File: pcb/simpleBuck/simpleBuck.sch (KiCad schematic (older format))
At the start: 55 parts

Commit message: Made lm2596 breakout board.
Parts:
- removed C? (x13): C, symbol Device:C
- removed D?: D_Zener, symbol Device:D_Zener
- removed D? (x3): D, symbol Device:D
- removed D?: INOLUX_IN-S63BTG, LEDs:LED_0603, symbol DBLS_Diode:INOLUX_IN-S63BTG
- removed J? (x3): Conn_01x02, symbol Connector_Generic:Conn_01x02
- removed L?: L, symbol Device:L
- removed Q?: Q_PMOS_GDS, symbol Device:Q_PMOS_GDS
- removed R?: SMD-RES-10K-0603, Resistors_SMD:R_0603, symbol DBLS_Resistor:SMD-RES-10K-0603
- removed R?: SMD-RES-0-0603, Resistors_SMD:R_0603, symbol DBLS_Resistor:SMD-RES-0-0603
- removed R? (x21): R, symbol Device:R
- removed RV? (x2): R_POT, symbol Device:R_POT
- removed SW?: SW_Push_SPDT, symbol Switch:SW_Push_SPDT
- removed U?: OP07, symbol Amplifier_Operational:OP07
- removed U?: LM2596S-ADJ, Package_TO_SOT_SMD:TO-263-5_TabPin3, symbol Regulator_Switching:LM2596S-ADJ
- removed U? (x3): LM2904, symbol Amplifier_Operational:LM2904
- removed U?: LP5912, DBLS_SON:WSON-6-1EP_2x2mm_P0.65mm_EP1x1.6mm_ThermalVias, symbol DBLS_LDO:LP5912
- added C? (x8): C, symbol Device:C
- added C?: PANASONIC_EEV-FK1J471M, Capacitors_SMD:CP_Elec_10x10.5, symbol DBLS_Capacitor:PANASONIC_EEV-FK1J471M
- added D? (x2): D, symbol Device:D
- added D?: ROHM_RSX501LAM20TR, Diodes_SMD:D_SMB_Handsoldering, symbol DBLS_Diode:ROHM_RSX501LAM20TR
- added D?: D_Zener, symbol Device:D_Zener
- added J? (x2): Conn_01x02, symbol Connector_Generic:Conn_01x02
- added L?: BOURNS_SRR1260A-330M, Inductors_SMD:L_12x12mm_h8mm, symbol DBLS_Inductor:BOURNS_SRR1260A-330M
- added Q?: Q_PMOS_GDS, symbol Device:Q_PMOS_GDS
- added R?: SMD-RES-0-0603, Resistors_SMD:R_0603, symbol DBLS_Resistor:SMD-RES-0-0603
- added R? (x20): R, symbol Device:R
- added R? (x2): VISHAYDALE_CRCW04020000Z0EDHP, Resistors_SMD:R_0402, symbol DBLS_Resistor:VISHAYDALE_CRCW04020000Z0EDHP
- added R?: SMD-RES-10K-0603, Resistors_SMD:R_0603, symbol DBLS_Resistor:SMD-RES-10K-0603
- added RV? (x2): R_POT, symbol Device:R_POT
- added SW?: SW_Push_SPDT, symbol Switch:SW_Push_SPDT
- added U?: LM2596S-ADJ, Package_TO_SOT_SMD:TO-263-5_TabPin3, symbol Regulator_Switching:LM2596S-ADJ
- added U? (x3): LM2904, symbol Amplifier_Operational:LM2904
- added U?: INA194, Package_TO_SOT_SMD:SOT-23-5, symbol Amplifier_Current:INA194
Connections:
- wire segments 126 -> 120
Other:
- note added: "-footprint is wrong\n-Backup cap??"
- note added: "D/L Footprints are close, \nbut not done\n"

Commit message: v1 - placed order with OSH park
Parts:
- removed C? (x8): C, symbol Device:C
- removed C?: PANASONIC_EEV-FK1J471M, Capacitors_SMD:CP_Elec_10x10.5, symbol DBLS_Capacitor:PANASONIC_EEV-FK1J471M
- removed D? (x2): D, symbol Device:D
- removed D?: ROHM_RSX501LAM20TR, Diodes_SMD:D_SMB_Handsoldering, symbol DBLS_Diode:ROHM_RSX501LAM20TR
- removed J?: Conn_01x02, symbol Connector_Generic:Conn_01x02
- removed L?: BOURNS_SRR1260A-330M, Inductors_SMD:L_12x12mm_h8mm, symbol DBLS_Inductor:BOURNS_SRR1260A-330M
- removed R?: SMD-RES-0-0603, Resistors_SMD:R_0603, symbol DBLS_Resistor:SMD-RES-0-0603
- removed R? (x20): R, symbol Device:R
- removed R? (x2): VISHAYDALE_CRCW04020000Z0EDHP, Resistors_SMD:R_0402, symbol DBLS_Resistor:VISHAYDALE_CRCW04020000Z0EDHP
- removed RV? (x2): R_POT, symbol Device:R_POT
- removed SW?: SW_Push_SPDT, symbol Switch:SW_Push_SPDT
- removed U?: LM2596S-ADJ, Package_TO_SOT_SMD:TO-263-5_TabPin3, symbol Regulator_Switching:LM2596S-ADJ
- removed U? (x3): LM2904, symbol Amplifier_Operational:LM2904
- removed U?: INA194, Package_TO_SOT_SMD:SOT-23-5, symbol Amplifier_Current:INA194
- added R?: STACKPOLE_CSRT2512FT50L0-UP, Resistors_SMD:R_2512, symbol DBLS_Resistor:STACKPOLE_CSRT2512FT50L0-UP
- added TP? (x2): DBLS_TESTPOINT_NORMAL, DBLS_Misc:DBLS_Testpoint_Normal, symbol DBLS_Misc:DBLS_TESTPOINT_NORMAL
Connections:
- net labels added: VBUS
- net labels removed: +5V, I_SENSE, VIN_PROT, VOUT, V_FB
- wire segments 120 -> 16
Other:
- note removed: "-footprint is wrong\n-Backup cap??"
- note removed: "D/L Footprints are close, \nbut not done\n"
- note removed: "EXTERNAL SWITCH"
- note removed: "SHOULD THIS BE 5V?"
- moved on the sheet: J?

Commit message: Added lm2596 and DACS + prelim layout.
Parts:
- removed D?: D_Zener, symbol Device:D_Zener
- removed J?: Conn_01x02, symbol Connector_Generic:Conn_01x02
- removed Q?: Q_PMOS_GDS, symbol Device:Q_PMOS_GDS
- removed R?: SMD-RES-10K-0603, Resistors_SMD:R_0603, symbol DBLS_Resistor:SMD-RES-10K-0603
- removed R?: STACKPOLE_CSRT2512FT50L0-UP, Resistors_SMD:R_2512, symbol DBLS_Resistor:STACKPOLE_CSRT2512FT50L0-UP
- removed TP? (x2): DBLS_TESTPOINT_NORMAL, DBLS_Misc:DBLS_Testpoint_Normal, symbol DBLS_Misc:DBLS_TESTPOINT_NORMAL
- added C1, C2: MURATA_GRT31CR61H106KE01L, Capacitors_SMD:C_1206, symbol DBLS_Capacitor:MURATA_GRT31CR61H106KE01L
- added C10, C11, C17, C18, C19, C20, C8, C9: MURATA_GCJ188R91H104KA01D, Capacitors_SMD:C_0603, symbol DBLS_Capacitor:MURATA_GCJ188R91H104KA01D
- added C12, C13, C3, C4, C5, C6: KEMET_C0603C103K5RAL7867, Capacitors_SMD:C_0603, symbol DBLS_Capacitor:KEMET_C0603C103K5RAL7867
- added C14: RUBYCON_100ZLH100MEFC10X20, Capacitors_THT:CP_Radial_D10.0mm_P5.00mm, symbol DBLS_Capacitor:RUBYCON_100ZLH100MEFC10X20
- added C15: MURATA_GCM155R71E103KA37D, Capacitors_SMD:C_0402, symbol DBLS_Capacitor:MURATA_GCM155R71E103KA37D
- added C16: PANASONIC_EEU-FC1H221B, Capacitors_THT:CP_Radial_D10.0mm_P5.00mm, symbol DBLS_Capacitor:PANASONIC_EEU-FC1H221B
- added C7: MURATA_KRM55WR7YA476MH01L, Capacitors_SMD:C_2220, symbol DBLS_Capacitor:MURATA_KRM55WR7YA476MH01L
- added D1, D2, D3: MICRO_COMMERCIAL_1N4148X-TP, LEDs:LED_0603, symbol DBLS_Diode:MICRO_COMMERCIAL_1N4148X-TP
- added D4: VISHAY_SSA34HE3_A_I, Diodes_SMD:D_SMA, symbol DBLS_Diode:VISHAY_SSA34HE3_A_I
- added J1, J3: Conn_01x04, Pin_Headers:Pin_Header_Straight_1x04_Pitch2.54mm, symbol Connector_Generic:Conn_01x04
- added J2: Conn_01x06, Pin_Headers:Pin_Header_Straight_1x06_Pitch2.54mm, symbol Connector_Generic:Conn_01x06
- added J4, J5, J6: Conn_01x02, Pin_Headers:Pin_Header_Straight_1x02_Pitch2.54mm, symbol Connector_Generic:Conn_01x02
- added JP1: PAD_JUMPER_2PIN_NC, DBLS_Misc:PAD_JUMPER_2PIN_NC, symbol DBLS_Misc:PAD_JUMPER_2PIN_NC
- added JP2, JP3, JP4, JP5, JP6, JP7, JP8: PAD_JUMPER_2PIN_0603, DBLS_Misc:PAD_JUMPER_2PIN_0603, symbol DBLS_Misc:PAD_JUMPER_2PIN_0603
- added L1: BOURNS_SRR1260A-330M, Inductors_SMD:L_12x12mm_h8mm, symbol DBLS_Inductor:BOURNS_SRR1260A-330M
- added Q1: TRANSISTOR_PNPMMBT4403, TO_SOT_Packages_SMD:SOT-23, symbol SparkFun-DiscreteSemi:TRANSISTOR_PNPMMBT4403
- added R1, R10, R2, R3, R6: VISHAYDALE_CRCW04021M00FKEDC, Resistors_SMD:R_0402, symbol DBLS_Resistor:VISHAYDALE_CRCW04021M00FKEDC
- added R11: SMD-RES-1.0K-0603, Resistors_SMD:R_0603, symbol DBLS_Resistor:SMD-RES-1.0K-0603
- added R12: VISHAYDALE_CRCW0402150KFKEDC, Resistors_SMD:R_0402, symbol DBLS_Resistor:VISHAYDALE_CRCW0402150KFKEDC
- added R13: STACKPOLE_CSRT2512FT50L0-UP, Resistors_SMD:R_2512, symbol DBLS_Resistor:STACKPOLE_CSRT2512FT50L0-UP
- added R14: VISHAYDALE_CRCW040268K0FKEDC, Resistors_SMD:R_0402, symbol DBLS_Resistor:VISHAYDALE_CRCW040268K0FKEDC
- added R4, R5, R7, R8, R9: VISHAY_CRCW060310K0FKEBC, Resistors_SMD:R_0603, symbol DBLS_Resistor:VISHAY_CRCW060310K0FKEBC
- added RV1, RV2: BOURNS_PV37W203C01B00, Potentiometers:Potentiometer_Trimmer_Bourns_3299Y, symbol DBLS_Resistor:BOURNS_PV37W203C01B00
- added TP1, TP2, TP3: DBLS_TESTPOINT_NORMAL, DBLS_Misc:DBLS_Testpoint_Normal, symbol DBLS_Misc:DBLS_TESTPOINT_NORMAL
- added U1: TI_INA181A2, TO_SOT_Packages_SMD:SOT-23-6, symbol DBLS_Amplifier:TI_INA181A2
- added U2, U3: TI_TL072HIDBVR, Housings_SOIC:SOIC-8_3.9x4.9mm_Pitch1.27mm, symbol DBLS_Amplifier:TI_TL072HIDBVR
- added U4: NATIONALSEMI_LM2596SX-ADJ, TO_SOT_Packages_SMD:TO-263-5_TabPin6, symbol DBLS_Regulator:NATIONALSEMI_LM2596SX-ADJ
- added U5, U6: ANALOG_MAX539BCSA+, Housings_SOIC:SOIC-8_3.9x4.9mm_Pitch1.27mm, symbol DBLS_Data_Converters:ANALOG_MAX539BCSA+
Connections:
- net labels added: +5VA, -5VA, ENABLE, I_ADC, I_SET, SCLK, SDIN, SYNC, VDD, VOUT, VOUT_HI, V_ADC, V_FB, V_SET
- net labels removed: VBUS
- wire segments 16 -> 178
- no-connect marks 0 -> 1
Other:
- note added: "3A"
- note added: "TODO: Calculate the right LC filter"
- note added: "TODO: Move R4 this to other side of caps"

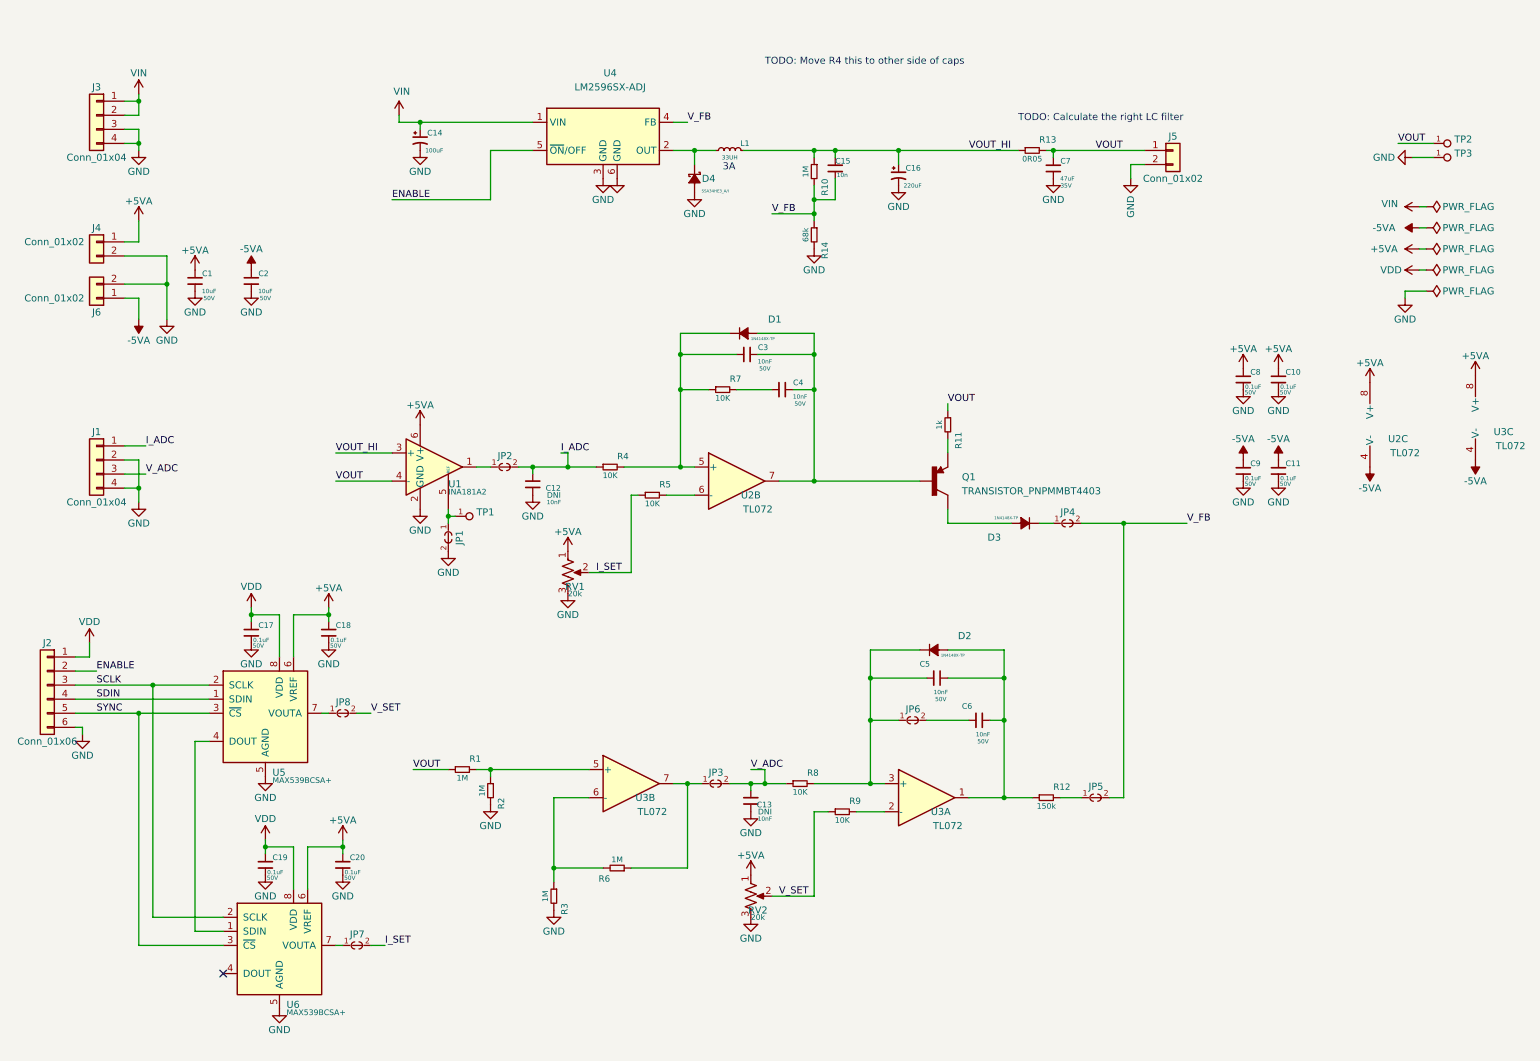
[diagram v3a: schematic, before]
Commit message: Updated schematic to include lm2596 on board.
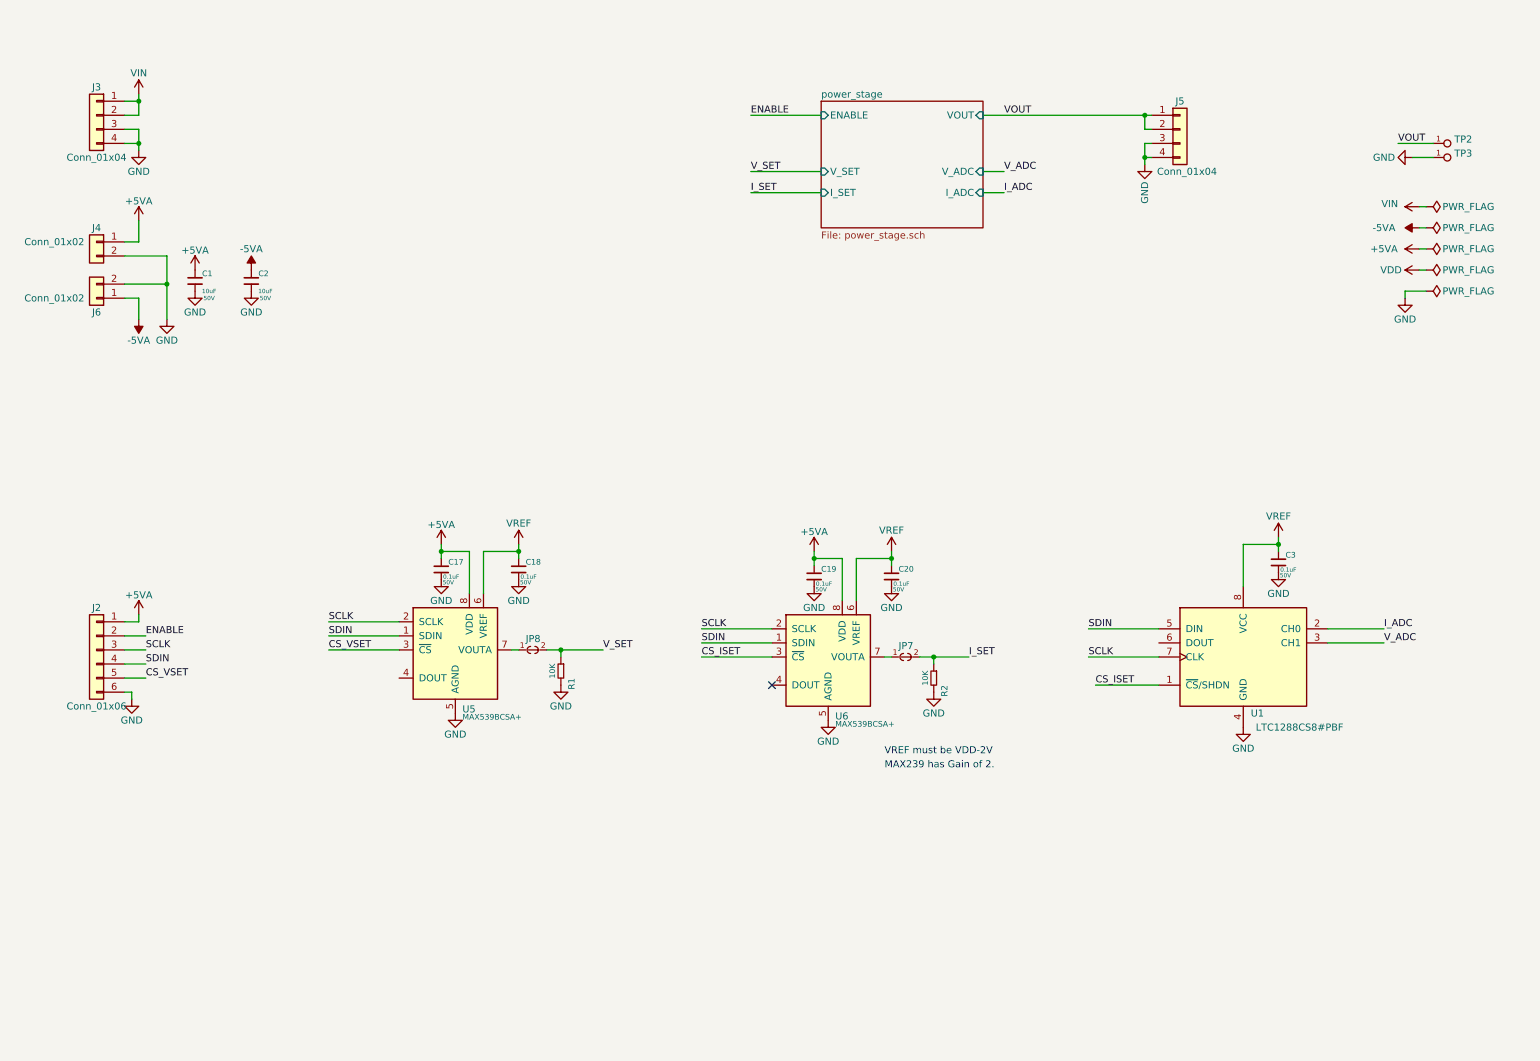
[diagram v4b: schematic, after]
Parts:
- removed C10, C11, C8, C9: MURATA_GCJ188R91H104KA01D, Capacitors_SMD:C_0603, symbol DBLS_Capacitor:MURATA_GCJ188R91H104KA01D
- removed C12, C13, C3, C4, C5, C6: KEMET_C0603C103K5RAL7867, Capacitors_SMD:C_0603, symbol DBLS_Capacitor:KEMET_C0603C103K5RAL7867
- removed C14: RUBYCON_100ZLH100MEFC10X20, Capacitors_THT:CP_Radial_D10.0mm_P5.00mm, symbol DBLS_Capacitor:RUBYCON_100ZLH100MEFC10X20
- removed C15: MURATA_GCM155R71E103KA37D, Capacitors_SMD:C_0402, symbol DBLS_Capacitor:MURATA_GCM155R71E103KA37D
- removed C16: PANASONIC_EEU-FC1H221B, Capacitors_THT:CP_Radial_D10.0mm_P5.00mm, symbol DBLS_Capacitor:PANASONIC_EEU-FC1H221B
- removed C7: MURATA_KRM55WR7YA476MH01L, Capacitors_SMD:C_2220, symbol DBLS_Capacitor:MURATA_KRM55WR7YA476MH01L
- removed D1, D2, D3: MICRO_COMMERCIAL_1N4148X-TP, LEDs:LED_0603, symbol DBLS_Diode:MICRO_COMMERCIAL_1N4148X-TP
- removed D4: VISHAY_SSA34HE3_A_I, Diodes_SMD:D_SMA, symbol DBLS_Diode:VISHAY_SSA34HE3_A_I
- removed J1: Conn_01x04, Pin_Headers:Pin_Header_Straight_1x04_Pitch2.54mm, symbol Connector_Generic:Conn_01x04
- removed J5: Conn_01x02, Pin_Headers:Pin_Header_Straight_1x02_Pitch2.54mm, symbol Connector_Generic:Conn_01x02
- removed JP1: PAD_JUMPER_2PIN_NC, DBLS_Misc:PAD_JUMPER_2PIN_NC, symbol DBLS_Misc:PAD_JUMPER_2PIN_NC
- removed JP2, JP3, JP4, JP5, JP6: PAD_JUMPER_2PIN_0603, DBLS_Misc:PAD_JUMPER_2PIN_0603, symbol DBLS_Misc:PAD_JUMPER_2PIN_0603
- removed L1: BOURNS_SRR1260A-330M, Inductors_SMD:L_12x12mm_h8mm, symbol DBLS_Inductor:BOURNS_SRR1260A-330M
- removed Q1: TRANSISTOR_PNPMMBT4403, TO_SOT_Packages_SMD:SOT-23, symbol SparkFun-DiscreteSemi:TRANSISTOR_PNPMMBT4403
- removed R1, R10, R2, R3, R6: VISHAYDALE_CRCW04021M00FKEDC, Resistors_SMD:R_0402, symbol DBLS_Resistor:VISHAYDALE_CRCW04021M00FKEDC
- removed R11: SMD-RES-1.0K-0603, Resistors_SMD:R_0603, symbol DBLS_Resistor:SMD-RES-1.0K-0603
- removed R12: VISHAYDALE_CRCW0402150KFKEDC, Resistors_SMD:R_0402, symbol DBLS_Resistor:VISHAYDALE_CRCW0402150KFKEDC
- removed R13: STACKPOLE_CSRT2512FT50L0-UP, Resistors_SMD:R_2512, symbol DBLS_Resistor:STACKPOLE_CSRT2512FT50L0-UP
- removed R14: VISHAYDALE_CRCW040268K0FKEDC, Resistors_SMD:R_0402, symbol DBLS_Resistor:VISHAYDALE_CRCW040268K0FKEDC
- removed R4, R5, R7, R8, R9: VISHAY_CRCW060310K0FKEBC, Resistors_SMD:R_0603, symbol DBLS_Resistor:VISHAY_CRCW060310K0FKEBC
- removed RV1, RV2: BOURNS_PV37W203C01B00, Potentiometers:Potentiometer_Trimmer_Bourns_3299Y, symbol DBLS_Resistor:BOURNS_PV37W203C01B00
- removed TP1: DBLS_TESTPOINT_NORMAL, DBLS_Misc:DBLS_Testpoint_Normal, symbol DBLS_Misc:DBLS_TESTPOINT_NORMAL
- removed U1: TI_INA181A2, TO_SOT_Packages_SMD:SOT-23-6, symbol DBLS_Amplifier:TI_INA181A2
- removed U2, U3: TI_TL072HIDBVR, Housings_SOIC:SOIC-8_3.9x4.9mm_Pitch1.27mm, symbol DBLS_Amplifier:TI_TL072HIDBVR
- removed U4: NATIONALSEMI_LM2596SX-ADJ, TO_SOT_Packages_SMD:TO-263-5_TabPin6, symbol DBLS_Regulator:NATIONALSEMI_LM2596SX-ADJ
- added C3: MURATA_GCJ188R91H104KA01D, Capacitors_SMD:C_0603, symbol DBLS_Capacitor:MURATA_GCJ188R91H104KA01D
- added J5: Conn_01x04, Pin_Headers:Pin_Header_Straight_1x04_Pitch2.54mm, symbol Connector_Generic:Conn_01x04
- added R1, R2: VISHAY_CRCW060310K0FKEBC, Resistors_SMD:R_0603, symbol DBLS_Resistor:VISHAY_CRCW060310K0FKEBC
- added U1: ANALOG_LTC1288CS8#PBF, Housings_SOIC:SOIC-8_3.9x4.9mm_Pitch1.27mm, symbol DBLS_Data_Converters:ANALOG_LTC1288CS8#PBF
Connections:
- net +5VA: now also C17.1, C19.1, J2.1 (Pin_1), U5.8 (VDD), U6.8 (VDD); no longer C18.1, C20.1, U5.6 (VREF), U6.6 (VREF)
- net GND: now also C3.2, J5.3 (Pin_3), J5.4 (Pin_4), R1.2, R2.2, U1.4 (GND)
- net I_ADC: now also U1.2 (CH0)
- net I_SET: now also R2.1
- net SCLK: now also U1.7 (CLK)
- net SDIN: now also U6.1 (SDIN), U1.5 (DIN)
- net VDD: no longer C17.1, C19.1, J2.1 (Pin_1), U5.8 (VDD), U6.8 (VDD)
- net VOUT: now also J5.1 (Pin_1), J5.2 (Pin_2)
- net V_ADC: now also U1.3 (CH1)
- net V_SET: now also R1.1
- net at U5.4 (DOUT): no longer U6.1 (SDIN)
- net SYNC renamed CS_VSET
- net CS_VSET: no longer U6.3 (~CS)
- new net CS_ISET: U1.1 (~CS~/SHDN), U6.3 (~CS)
- new net VREF: C18.1, C20.1, C3.1, U1.8 (VCC), U5.6 (VREF), U6.6 (VREF)
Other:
- note added: "MAX239 has Gain of 2."
- note added: "VREF must be VDD-2V"
- note removed: "3A"
- note removed: "TODO: Calculate the right LC filter"
- note removed: "TODO: Move R4 this to other side of caps"
- moved on the sheet: C17, C18, C19, C20, J2, JP7, JP8, U5, U6
